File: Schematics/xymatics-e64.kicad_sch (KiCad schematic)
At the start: 128 parts, among them J12 STM32 SWD, J13 X-STOP, J14 Y-STOP, J15 Z-STOP, J16 5V POWER, J17 CAN1, J18 CAN2, J19 CAN3, J20 CAN4, J21 CAN5, J22 CAN6, J23 CAN7, J24 CAN8, J25 FAN1, J27 FAN2, J28 FAN3, J29 FAN4, J30 FAN5, J32 HEATBED, J35 BED THERMISTOR, Q1 HEATBED, Q2 FAN1, Q3 FAN2, Q4 FAN3, Q5 FAN4, Q6 FAN5, SW2 STM32 RESET, SW3 STM32 BOOT, U10 STM32F407VET6, U11 MOTOR A, U12 MOTOR B, U13 MOTOR Z1, U14 MOTOR Z2, U15 MOTOR Z3, U16 TPS54302, U17 AMS1117CD-3.3, U18 TJA1051T-3, U28 74LVC1G17, Y2 16MHZ

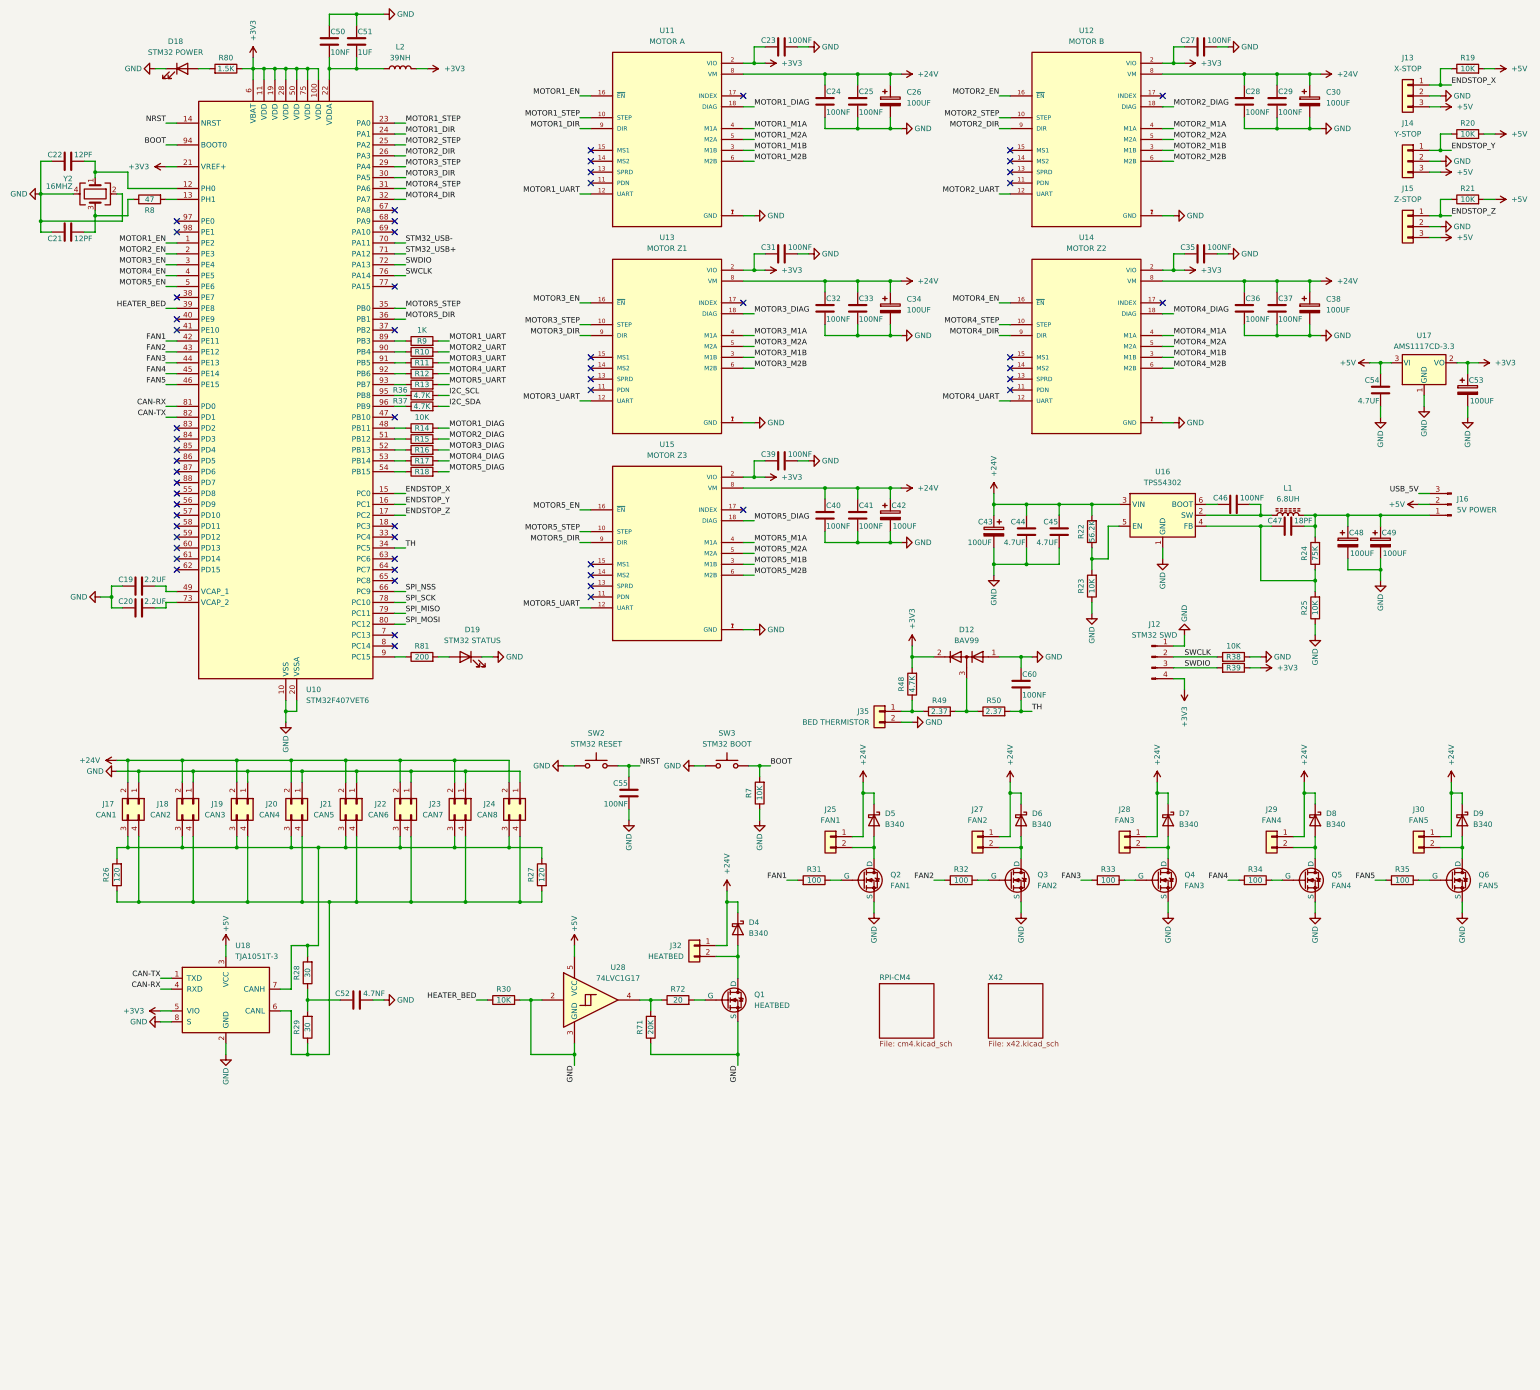
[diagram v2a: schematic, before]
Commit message: Update E64 schematics
Finish E64 PCB
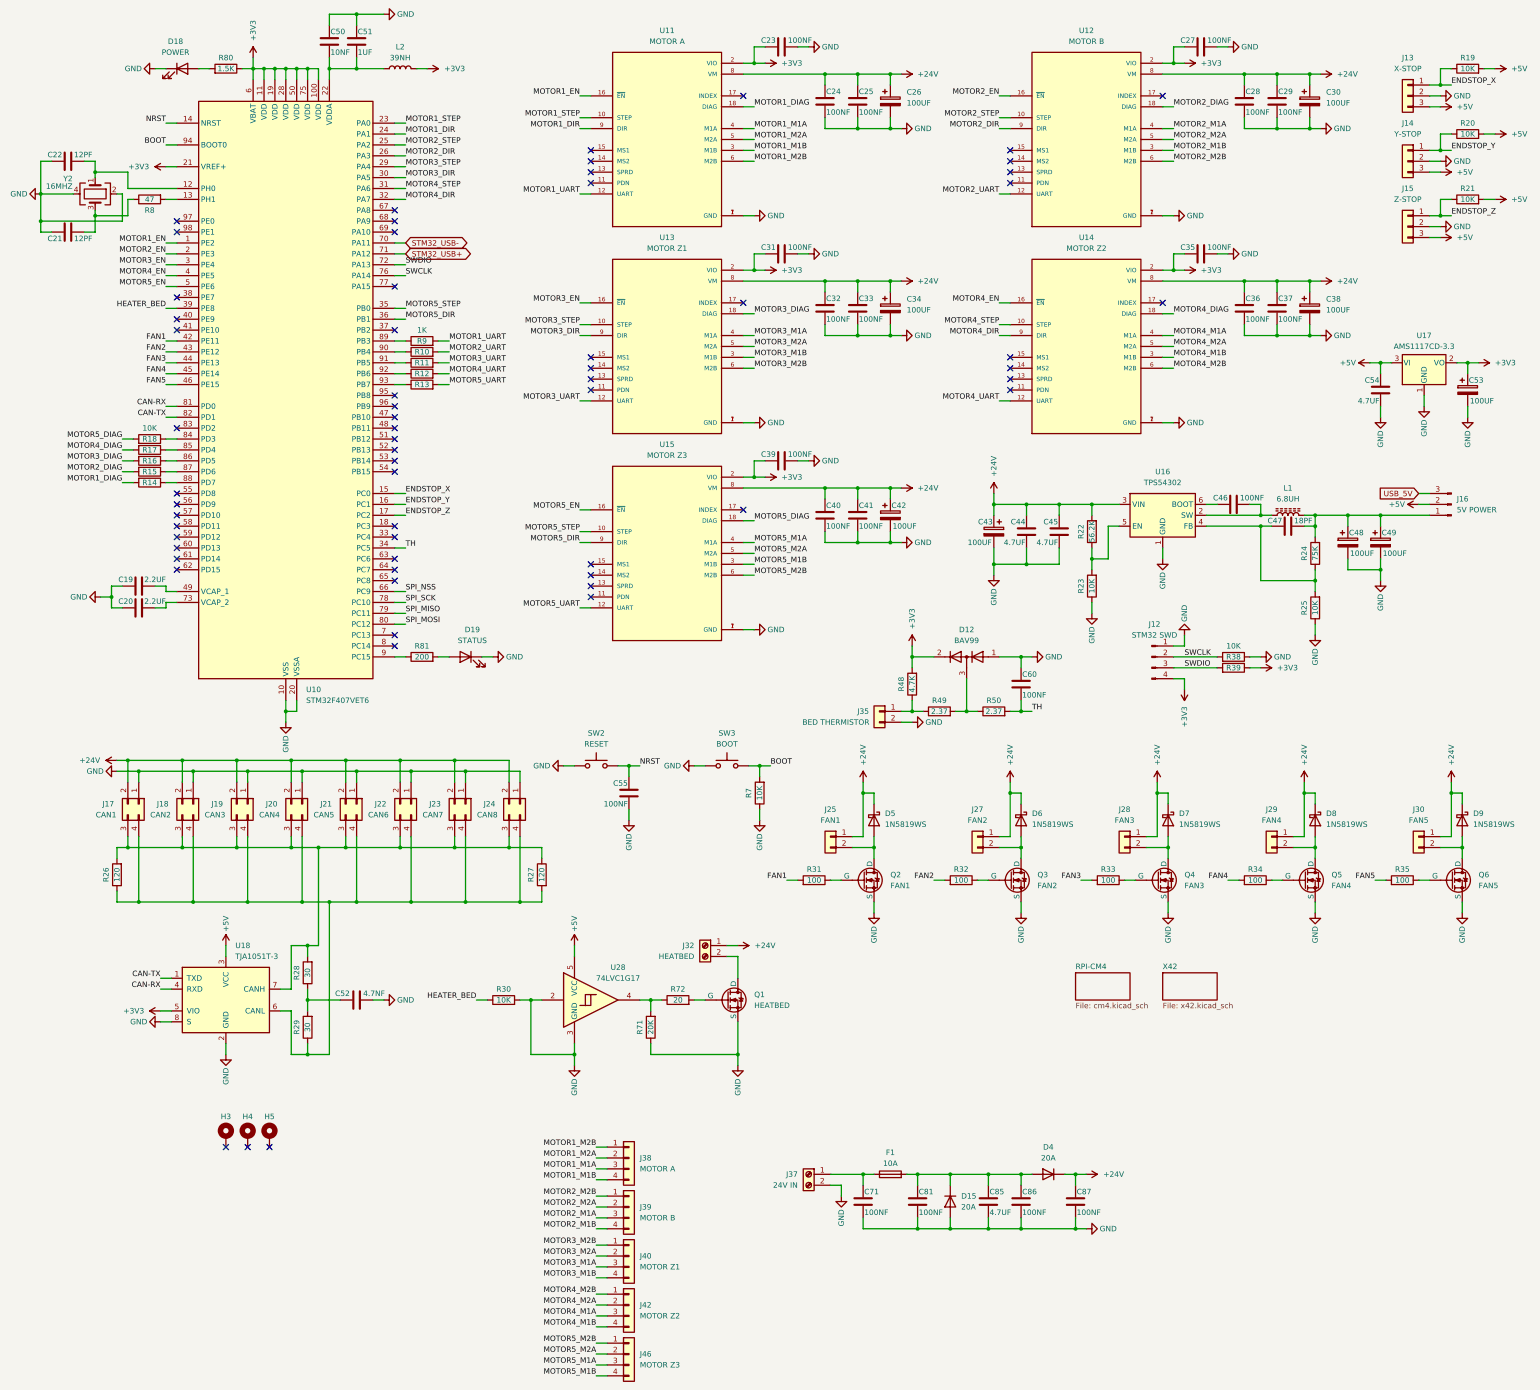
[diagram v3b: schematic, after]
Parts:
- removed D4, D5, D6, D7, D8, D9: B340, Diode_SMD:D_SMC, symbol Diode:B340
- removed J32: HEATBED, Connector_JST:JST_XH_B2B-XH-A_1x02_P2.50mm_Vertical, symbol Connector_Generic:Conn_01x02
- removed R36, R37: 4.7K, Resistor_SMD:R_0805_2012Metric, symbol Device:R
- added C71, C81, C86, C87: 100NF, Capacitor_SMD:C_0805_2012Metric, symbol Device:C
- added C85: 4.7UF, Capacitor_SMD:C_0805_2012Metric, symbol Device:C
- added D15, D4: 20A, Diode_SMD:D_SMB, symbol Device:D
- added D5, D6, D7, D8, D9: 1N5819WS, Diode_SMD:D_SOD-323, symbol Diode:1N5819WS
- added F1: 10A, Fuse:Fuse_Blade_ATO_directSolder, symbol Device:Fuse
- added H3, H4, H5: MountingHole_Pad, MountingHole:MountingHole_3mm_Pad, symbol Mechanical:MountingHole_Pad
- added J32: HEATBED, TerminalBlock:TerminalBlock_MaiXu_MX126-5.0-02P_1x02_P5.00mm, symbol Connector:Screw_Terminal_01x02
- added J37: 24V IN, TerminalBlock:TerminalBlock_MaiXu_MX126-5.0-02P_1x02_P5.00mm, symbol Connector:Screw_Terminal_01x02
- added J38: MOTOR A, Connector_JST:JST_XH_B4B-XH-A_1x04_P2.50mm_Vertical, symbol Connector_Generic:Conn_01x04
- added J39: MOTOR B, Connector_JST:JST_XH_B4B-XH-A_1x04_P2.50mm_Vertical, symbol Connector_Generic:Conn_01x04
- added J40: MOTOR Z1, Connector_JST:JST_XH_B4B-XH-A_1x04_P2.50mm_Vertical, symbol Connector_Generic:Conn_01x04
- added J42: MOTOR Z2, Connector_JST:JST_XH_B4B-XH-A_1x04_P2.50mm_Vertical, symbol Connector_Generic:Conn_01x04
- added J46: MOTOR Z3, Connector_JST:JST_XH_B4B-XH-A_1x04_P2.50mm_Vertical, symbol Connector_Generic:Conn_01x04
- D18: value STM32 POWER -> POWER
- D19: value STM32 STATUS -> STATUS
- R24: footprint Resistor_SMD:R_0805_2012Metric -> Resistor_SMD:R_1206_3216Metric
- SW2: value STM32 RESET -> RESET
- SW3: value STM32 BOOT -> BOOT
- U17: footprint Package_TO_SOT_SMD:TO-252-3_TabPin2 -> Package_TO_SOT_SMD:TO-252-2
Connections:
- net +24V: now also C87.1, D4.1 (K), D5.1 (K), D6.1 (K), D7.1 (K), D8.1 (K), D9.1 (K), J32.1 (Pin_1)
- net GND: now also C71.2, C81.2, C85.2, C86.2, C87.2, D15.2 (A), J37.2 (Pin_2)
- net MOTOR1_M1A: now also J38.3 (Pin_3)
- net MOTOR1_M1B: now also J38.4 (Pin_4)
- net MOTOR1_M2A: now also J38.2 (Pin_2)
- net MOTOR1_M2B: now also J38.1 (Pin_1)
- net MOTOR2_M1A: now also J39.3 (Pin_3)
- net MOTOR2_M1B: now also J39.4 (Pin_4)
- net MOTOR2_M2A: now also J39.2 (Pin_2)
- net MOTOR2_M2B: now also J39.1 (Pin_1)
- net MOTOR3_M1A: now also J40.3 (Pin_3)
- net MOTOR3_M1B: now also J40.4 (Pin_4)
- net MOTOR3_M2A: now also J40.2 (Pin_2)
- net MOTOR3_M2B: now also J40.1 (Pin_1)
- net MOTOR4_M1A: now also J42.3 (Pin_3)
- net MOTOR4_M1B: now also J42.4 (Pin_4)
- net MOTOR4_M2A: now also J42.2 (Pin_2)
- net MOTOR4_M2B: now also J42.1 (Pin_1)
- net MOTOR5_M1A: now also J46.3 (Pin_3)
- net MOTOR5_M1B: now also J46.4 (Pin_4)
- net MOTOR5_M2A: now also J46.2 (Pin_2)
- net MOTOR5_M2B: now also J46.1 (Pin_1)
- net at J30.2 (Pin_2), Q6.1 (D): now also D9.2 (A)
- net at J27.2 (Pin_2), Q3.1 (D): now also D6.2 (A)
- net at Q1.1 (G): now also R72.2
- net at J29.2 (Pin_2), Q5.1 (D): now also D8.2 (A)
- net at R16.1: now also U10.86 (PD5); no longer U10.52 (PB13)
- net at J25.2 (Pin_2), Q2.1 (D): now also D5.2 (A)
- net at Q1.2 (D): now also J32.2 (Pin_2); no longer R72.2
- net at R14.1: now also U10.88 (PD7); no longer U10.48 (PB11)
- net at R17.1: now also U10.85 (PD4); no longer U10.53 (PB14)
- net at J28.2 (Pin_2), Q4.1 (D): now also D7.2 (A)
- net at R18.1: now also U10.84 (PD3); no longer U10.54 (PB15)
- net at R15.1: now also U10.87 (PD6); no longer U10.51 (PB12)
- new net: C71.1, F1.1, J37.1 (Pin_1)
- new net: C81.1, C85.1, C86.1, D15.1 (K), D4.2 (A), F1.2
- no-connect marks 57 -> 62
